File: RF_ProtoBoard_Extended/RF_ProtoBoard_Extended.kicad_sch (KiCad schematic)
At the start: 12 parts, among them J1 Screw_Terminal_01x02, J2 Conn_VPlus_Gnd

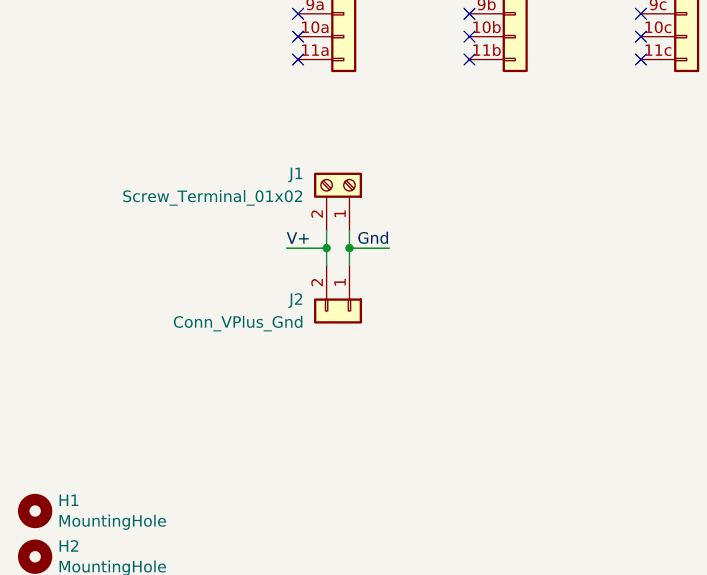
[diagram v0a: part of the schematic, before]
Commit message: Basic update.
Did basic power update. Would like to add an SOIC-8 or such of parts I normally use.
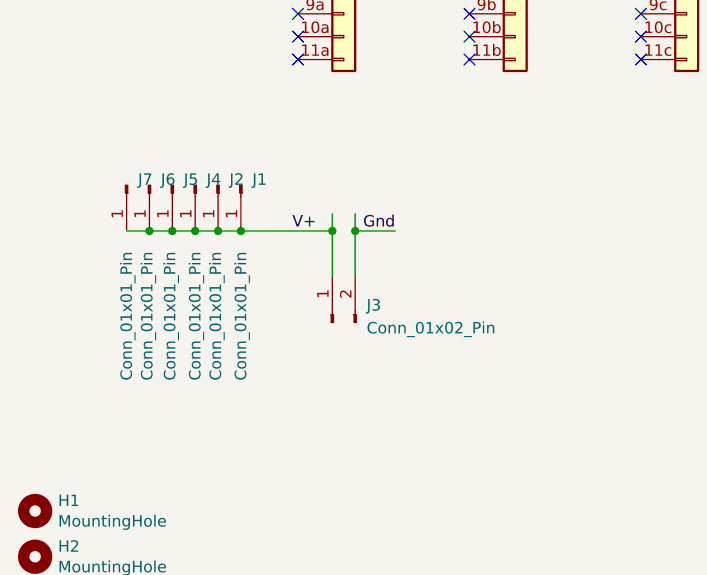
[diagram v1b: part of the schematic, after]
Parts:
- removed J1: Screw_Terminal_01x02, TerminalBlock_MetzConnect:TerminalBlock_MetzConnect_Type055_RT01502HDWU_1x02_P5.00mm_Horizontal, symbol Connector:Screw_Terminal_01x02
- removed J2: Conn_VPlus_Gnd, RF_ProtoBoard:VPlus_Gnd_Pads, symbol RF_ProtoBoard:Conn_VPlus_Gnd
- added J1, J2, J4, J5, J6, J7: Conn_01x01_Pin, Connector_Wire:SolderWire-1sqmm_1x01_D1.4mm_OD3.9mm, symbol Connector:Conn_01x01_Pin
- added J3: Conn_01x02_Pin, RF_ProtoBoard:CONN_SD-43650-001_02_MOL, symbol Connector:Conn_01x02_Pin
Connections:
- net Gnd: now also J3.2 (Pin_2)
- net V+: now also J1.1 (Pin_1), J2.1 (Pin_1), J3.1 (Pin_1), J4.1 (Pin_1), J5.1 (Pin_1), J6.1 (Pin_1), J7.1 (Pin_1)

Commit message: Ready to output.
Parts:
- removed J7: Conn_01x01_Pin, Connector_Wire:SolderWire-1sqmm_1x01_D1.4mm_OD3.9mm, symbol Connector:Conn_01x01_Pin
- added J10, J11, J12, J8, J9: Conn_01x01_Pin, Connector_Wire:SolderWire-0.75sqmm_1x01_D1.25mm_OD2.3mm, symbol Connector:Conn_01x01_Pin
- H1, H2, H3, H4: footprint RF_ProtoBoard:MountingHole_2.7mm_M2.5_Clearance_1.7mm -> MountingHole:MountingHole_3.2mm_M3
- J1, J2, J4, J5, J6: footprint Connector_Wire:SolderWire-1sqmm_1x01_D1.4mm_OD3.9mm -> Connector_Wire:SolderWire-0.75sqmm_1x01_D1.25mm_OD2.3mm
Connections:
- net Gnd: now also J10.1 (Pin_1), J11.1 (Pin_1), J12.1 (Pin_1), J8.1 (Pin_1), J9.1 (Pin_1)
